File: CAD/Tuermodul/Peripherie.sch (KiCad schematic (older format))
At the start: 43 parts, among them Q201 Q_NPN_CBE, Q202 Q_NPN_CBE, Q203 Q_NPN_CBE, Q204 Q_NPN_CBE, Q205 Q_NPN_CBE, Q206 Q_NPN_CBE, Q207 Q_NPN_CBE, Q208 Q_NPN_CBE, Q209 Q_PMOS_GDS, Q210 Q_PMOS_GDS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

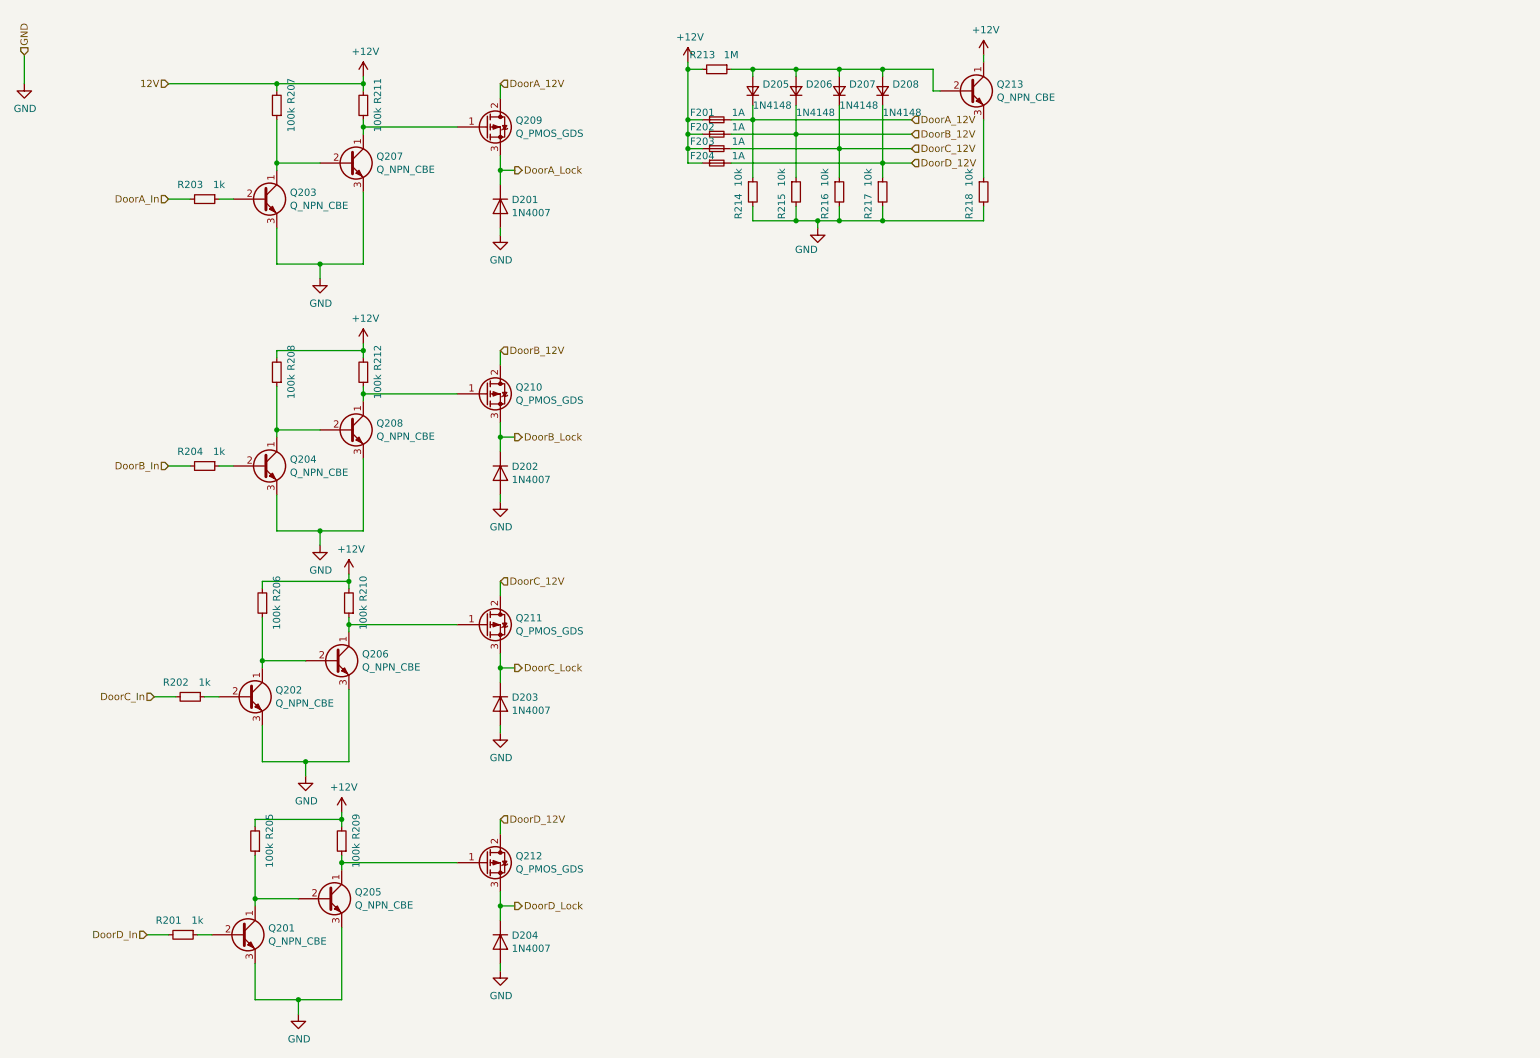
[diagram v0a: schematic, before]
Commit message: -add: Fuse Error, missing LEDs -mod: some Resistor footprints changed -mod: first placement in layout
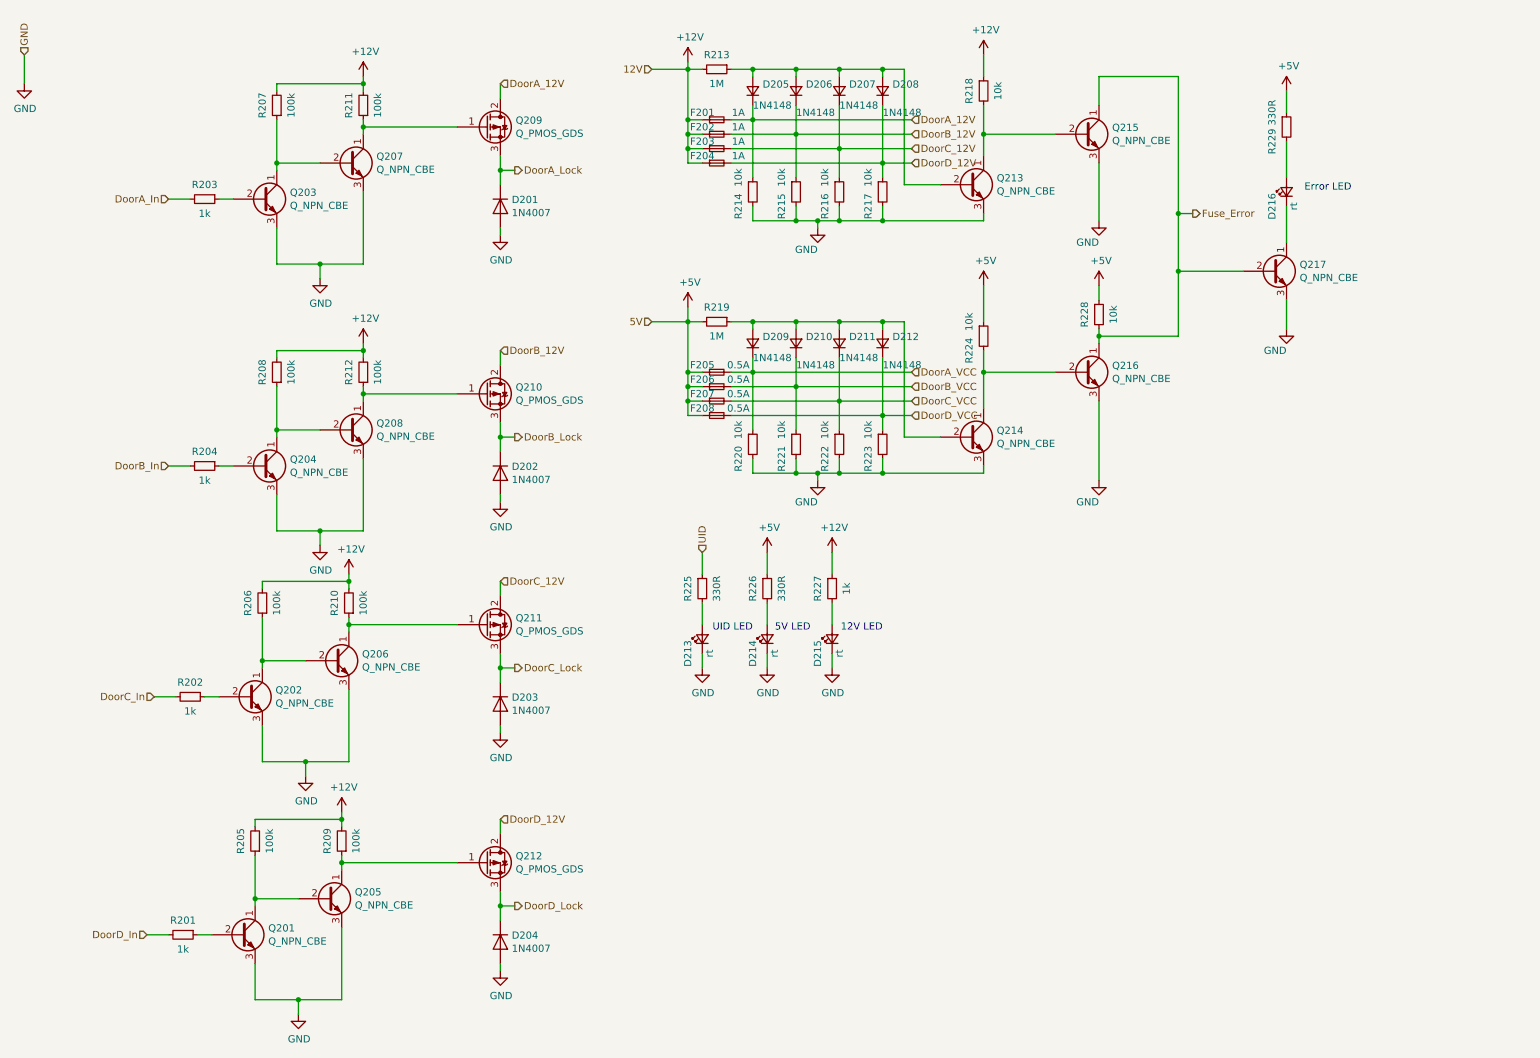
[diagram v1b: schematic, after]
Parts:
- added D209, D210, D211, D212: 1N4148, Diode_THT:D_DO-41_SOD81_P7.62mm_Horizontal, symbol Device:D_Small
- added D213, D214, D215, D216: rt, LED_THT:LED_D3.0mm, symbol Device:LED_Small
- added F205, F206, F207, F208: 0.5A, Fuse:Fuseholder_Cylinder-5x20mm_Schurter_0031_8201_Horizontal_Open, symbol Device:Fuse_Small
- added Q214, Q215, Q216, Q217: Q_NPN_CBE, Package_TO_SOT_THT:TO-92_HandSolder, symbol Device:Q_NPN_CBE
- added R219: 1M, Resistor_THT:R_Axial_DIN0207_L6.3mm_D2.5mm_P7.62mm_Horizontal, symbol Device:R_Small
- added R220, R221, R222, R223, R224, R228: 10k, Resistor_THT:R_Axial_DIN0207_L6.3mm_D2.5mm_P7.62mm_Horizontal, symbol Device:R_Small
- added R225, R226, R229: 330R, Resistor_THT:R_Axial_DIN0207_L6.3mm_D2.5mm_P7.62mm_Horizontal, symbol Device:R_Small
- added R227: 1k, Resistor_THT:R_Axial_DIN0207_L6.3mm_D2.5mm_P7.62mm_Horizontal, symbol Device:R_Small
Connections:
- net +12V: now also R218.1, R227.1; no longer Q213.1 (C)
- net GND: now also Q213.3 (E), D213.1 (K), D214.1 (K), D215.1 (K), Q214.3 (E), Q215.3 (E), Q216.3 (E), Q217.3 (E), R220.2, R221.2, R222.2, R223.2; no longer R218.2
- new net: Q213.1 (C), Q215.2 (B), R218.2
- new net: Q214.1 (C), Q216.2 (B), R224.2
- new net: D209.2 (A), D210.2 (A), D211.2 (A), D212.2 (A), Q214.2 (B), R219.1
- new net: D213.2 (A), R225.2
- new net: D216.1 (K), Q217.1 (C)
- new net: D216.2 (A), R229.2
- new net: D214.2 (A), R226.2
- new net: D215.2 (A), R227.2
- new net +5V: F205.1, F206.1, F207.1, F208.1, R219.2, R224.1, R226.1, R228.1, R229.1
- new net DoorA_VCC: D209.1 (K), F205.2, R220.1
- new net DoorB_VCC: D210.1 (K), F206.2, R221.1
- new net DoorC_VCC: D211.1 (K), F207.2, R222.1
- new net DoorD_VCC: D212.1 (K), F208.2, R223.1
- new net Fuse_Error: Q215.1 (C), Q216.1 (C), Q217.2 (B), R228.2
- new net UID: R225.1
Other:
- note added: "12V LED"
- note added: "5V LED"
- note added: "Error LED"
- note added: "UID LED"
- moved on the sheet: Q213, R218

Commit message: -add: Front.sch for front panel -mod: moved leds and switches to front panel -mod: added MK contacts (not finished jet) -mod: added switches
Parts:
- removed D213, D214, D215, D216: rt, LED_THT:LED_D3.0mm, symbol Device:LED_Small
- removed Q217: Q_NPN_CBE, Package_TO_SOT_THT:TO-92_HandSolder, symbol Device:Q_NPN_CBE
- removed R225, R226, R229: 330R, Resistor_THT:R_Axial_DIN0207_L6.3mm_D2.5mm_P7.62mm_Horizontal, symbol Device:R_Small
- removed R227: 1k, Resistor_THT:R_Axial_DIN0207_L6.3mm_D2.5mm_P7.62mm_Horizontal, symbol Device:R_Small
- added J201: Conn_02x25_Counter_Clockwise, Connector_IDC:IDC-Header_2x25_P2.54mm_Vertical, symbol Connector_Generic:Conn_02x25_Counter_Clockwise
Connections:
- net labels added: 3V3, DA_Rx, DA_Tx, DB_Rx, DB_Tx, DC_Rx, DC_Tx, DD_Rx, DD_Tx, DoorA_Auto, DoorA_MK, DoorB_Auto, DoorB_MK, DoorC_Auto, DoorC_MK, DoorD_Auto, DoorD_MK
- wire segments 221 -> 231
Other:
- note removed: "12V LED"
- note removed: "5V LED"
- note removed: "Error LED"
- note removed: "UID LED"
- moved on the sheet: D201, D202, D203, D204, D205, D206, D207, D208, D209, D210, D211, D212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

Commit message: -add: switch library for spdt switches -mod: improvements in schematic, bugfixes -mod: placement and routing of the ftdi chip + chicken food
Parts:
- removed Q201, Q202, Q203, Q204: Q_NPN_CBE, Package_TO_SOT_THT:TO-92_HandSolder, symbol Device:Q_NPN_CBE
- removed R205, R206, R207, R208: 100k, Resistor_THT:R_Axial_DIN0207_L6.3mm_D2.5mm_P7.62mm_Horizontal, symbol Device:R_Small
- removed R214, R215, R216, R217, R220, R221, R222, R223: 10k, Resistor_THT:R_Axial_DIN0207_L6.3mm_D2.5mm_P7.62mm_Horizontal, symbol Device:R_Small
- added D213, D214: 1N4148, Diode_THT:D_DO-41_SOD81_P7.62mm_Horizontal, symbol Device:D_Small
- added RN201, RN202: 4x10k, Resistor_THT:R_Array_SIP5, symbol Device:R_Network04
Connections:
- net labels removed: 3V3
- wire segments 231 -> 207
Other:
- moved on the sheet: D205, D206, D207, D208, D209, D210, D211, D212, F201, F202, F203, F204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

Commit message: -mod: adapted TechSpec due to power enable discussion -mod: changed pin header for front-to-main panel connection -mod: general layout work
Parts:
- removed J201: Conn_02x25_Counter_Clockwise, Connector_IDC:IDC-Header_2x25_P2.54mm_Vertical, symbol Connector_Generic:Conn_02x25_Counter_Clockwise
- added J201: Conn_02x20_Counter_Clockwise, Connector_PinSocket_2.54mm:PinSocket_2x20_P2.54mm_Vertical_SMD, symbol Connector_Generic:Conn_02x20_Counter_Clockwise
- added R205: 10k, Resistor_SMD:R_0603_1608Metric_Pad1.05x0.95mm_HandSolder, symbol Device:R_Small
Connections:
- net labels added: ~PWR_EN~
- net labels removed: UID
- wire segments 207 -> 212
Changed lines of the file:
@@
 F 3 "~" H 4150 1500 50  0001 C CNN
 	1    4150 1500
-	1    0    0    -1
+	1    0    0    1
 $EndComp
 $Comp
@@
 F 3 "~" H 4150 3350 50  0001 C CNN
 	1    4150 3350
-	1    0    0    -1
+	1    0    0    1
 $EndComp
 Wire Wire Line
@@
 F 3 "~" H 4150 4950 50  0001 C CNN
 	1    4150 4950
-	1    0    0    -1
+	1    0    0    1
 $EndComp
 Wire Wire Line
@@
 F 3 "~" H 4150 6600 50  0001 C CNN
 	1    4150 6600
-	1    0    0    -1
+	1    0    0    1
 $EndComp
 Wire Wire Line
@@
 $EndComp
 $Comp
-L power:GND #PWR?
-U 1 1 5C5F9E5C
-P 3300 4150
-AR Path="/5C5F9E5C" Ref="#PWR?"  Part="1"
-AR Path="/5C5BDAF5/5C5F9E5C" Ref="#PWR0204"  Part="1"
-F 0 "#PWR0204" H 3300 3900 50  0001 C CNN
-F 1 "GND" H 3305 3977 50  0000 C CNN
-F 2 "" H 3300 4150 50  0001 C CNN
-F 3 "" H 3300 4150 50  0001 C CNN
-	1    3300 4150
-	1    0    0    -1
-$EndComp
-$Comp
 L Device:Q_NPN_CBE Q?
 U 1 1 5C5F9E69
@@
 $EndComp
 $Comp
-L power:GND #PWR?
-U 1 1 5C5FAB97
-P 3300 5800
-AR Path="/5C5FAB97" Ref="#PWR?"  Part="1"
-AR Path="/5C5BDAF5/5C5FAB97" Ref="#PWR0202"  Part="1"
-F 0 "#PWR0202" H 3300 5550 50  0001 C CNN
-F 1 "GND" H 3305 5627 50  0000 C CNN
-F 2 "" H 3300 5800 50  0001 C CNN
-F 3 "" H 3300 5800 50  0001 C CNN
-	1    3300 5800
-	1    0    0    -1
-$EndComp
-$Comp
 L Device:R_Small R?
 U 1 1 5C5FABAA
@@
 $EndComp
 $Comp
-L power:GND #PWR?
-U 1 1 5C5FC3EB
-P 3300 7650
-AR Path="/5C5FC3EB" Ref="#PWR?"  Part="1"
-AR Path="/5C5BDAF5/5C5FC3EB" Ref="#PWR0201"  Part="1"
-F 0 "#PWR0201" H 3300 7400 50  0001 C CNN
-F 1 "GND" H 3305 7477 50  0000 C CNN
-F 2 "" H 3300 7650 50  0001 C CNN
-F 3 "" H 3300 7650 50  0001 C CNN
-	1    3300 7650
-	1    0    0    -1
-$EndComp
-$Comp
 L Device:Q_NPN_CBE Q?
 U 1 1 5C5FC3F8
@@
 Wire Wire Line
 	5300 1100 5550 1100
+Text HLabel 10100 4300 0    50   Input ~ 0
+DA_Tx
 Text HLabel 10100 4400 0    50   Input ~ 0
-DA_Tx
-Text HLabel 10100 4500 0    50   Input ~ 0
 DA_Rx
+Text HLabel 10800 4300 2    50   Input ~ 0
+DB_Tx
 Text HLabel 10800 4400 2    50   Input ~ 0
-DB_Tx
-Text HLabel 10800 4500 2    50   Input ~ 0
 DB_Rx
+Text HLabel 10100 5000 0    50   Input ~ 0
+DC_Tx
 Text HLabel 10100 5100 0    50   Input ~ 0
-DC_Tx
-Text HLabel 10100 5200 0    50   Input ~ 0
 DC_Rx
+Text HLabel 10800 5000 2    50   Input ~ 0
+DD_Tx
 Text HLabel 10800 5100 2    50   Input ~ 0
-DD_Tx
-Text HLabel 10800 5200 2    50   Input ~ 0
 DD_Rx
-$Comp
-L Connector_Generic:Conn_02x25_Counter_Clockwise J201
-U 1 1 5C5D89B8
-P 10400 5100
-F 0 "J201" H 10450 6517 50  0000 C CNN
-F 1 "Conn_02x25_Counter_Clockwise" H 10450 6426 50  0000 C CNN
-F 2 "Connector_IDC:IDC-Header_2x25_P2.54mm_Vertical" H 10400 5100 50  0001 C CNN
-F 3 "~" H 10400 5100 50  0001 C CNN
-	1    10400 5100
-	1    0    0    -1
-$EndComp
 $Comp
 L power:+12V #PWR?
@@
 Wire Wire Line
 	10200 4200 10150 4200
-Text HLabel 10150 4300 0    50   Input ~ 0
-UID
-Wire Wire Line
-	10200 4300 10150 4300
-Text HLabel 10100 4600 0    50   Output ~ 0
+Text HLabel 10100 4500 0    50   Output ~ 0
 DoorA_Lock
+Text HLabel 10100 4700 0    50   Input ~ 0
+DoorA_MK
 Text HLabel 10100 4800 0    50   Input ~ 0
-DoorA_MK
+DoorA_12V
 Text HLabel 10100 4900 0    50   Input ~ 0
-DoorA_12V
-Text HLabel 10100 5000 0    50   Input ~ 0
 DoorA_VCC
-Text HLabel 10800 4600 2    50   Output ~ 0
+Text HLabel 10800 4500 2    50   Output ~ 0
 DoorB_Lock
-Text HLabel 10100 5300 0    50   Output ~ 0
+Text HLabel 10100 5200 0    50   Output ~ 0
 DoorC_Lock
-Text HLabel 10800 5300 2    50   Output ~ 0
+Text HLabel 10800 5200 2    50   Output ~ 0
 DoorD_Lock
+Text HLabel 10800 4700 2    50   Input ~ 0
+DoorB_MK
+Text HLabel 10100 5400 0    50   Input ~ 0
+DoorC_MK
+Text HLabel 10800 5400 2    50   Input ~ 0
+DoorD_MK
 Text HLabel 10800 4800 2    50   Input ~ 0
-DoorB_MK
+DoorB_12V
 Text HLabel 10100 5500 0    50   Input ~ 0
-DoorC_MK
+DoorC_12V
 Text HLabel 10800 5500 2    50   Input ~ 0
-DoorD_MK
+DoorD_12V
 Text HLabel 10800 4900 2    50   Input ~ 0
-DoorB_12V
+DoorB_VCC
 Text HLabel 10100 5600 0    50   Input ~ 0
-DoorC_12V
+DoorC_VCC
 Text HLabel 10800 5600 2    50   Input ~ 0
-DoorD_12V
-Text HLabel 10800 5000 2    50   Input ~ 0
-DoorB_VCC
-Text HLabel 10100 5700 0    50   Input ~ 0
-DoorC_VCC
-Text HLabel 10800 5700 2    50   Input ~ 0
 DoorD_VCC
 Text HLabel 4350 1850 2    50   Input ~ 0
@@
 Wire Wire Line
 	4250 2000 4250 2100
-Text HLabel 10100 4700 0    50   Input ~ 0
+Text HLabel 10100 4600 0    50   Input ~ 0
 DoorA_Auto
-Text HLabel 10800 4700 2    50   Input ~ 0
+Text HLabel 10800 4600 2    50   Input ~ 0
 DoorB_Auto
-Text HLabel 10100 5400 0    50   Input ~ 0
+Text HLabel 10100 5300 0    50   Input ~ 0
 DoorC_Auto
-Text HLabel 10800 5400 2    50   Input ~ 0
+Text HLabel 10800 5300 2    50   Input ~ 0
 DoorD_Auto
 Wire Wire Line
@@
 	10100 5600 10200 5600
 Wire Wire Line
-	10100 5700 10200 5700
-Wire Wire Line
-	10800 5700 10700 5700
-Wire Wire Line
 	10700 5600 10800 5600
 Wire Wire Line
@@
 Wire Wire Line
 	9250 2100 9250 2950
-$Comp
-L power:GND #PWR?
-U 1 1 5C5C48A6
-P 3300 2450
-AR Path="/5C5C48A6" Ref="#PWR?"  Part="1"
-AR Path="/5C5BDAF5/5C5C48A6" Ref="#PWR0203"  Part="1"
-F 0 "#PWR0203" H 3300 2200 50  0001 C CNN
-F 1 "GND" H 3305 2277 50  0000 C CNN
-F 2 "" H 3300 2450 50  0001 C CNN
-F 3 "" H 3300 2450 50  0001 C CNN
-	1    3300 2450
-	1    0    0    -1
-$EndComp
 Wire Wire Line
 	3300 7050 3300 7650
@@
 Wire Wire Line
 	6300 3600 6300 3650
+Text HLabel 3200 2450 0    50   Input ~ 0
+~PWR_EN~
+Text HLabel 3200 4150 0    50   Input ~ 0
+~PWR_EN~
+Text HLabel 3200 5800 0    50   Input ~ 0
+~PWR_EN~
+Text HLabel 3200 7650 0    50   Input ~ 0
+~PWR_EN~
+Text HLabel 1400 1300 3    50   Input ~ 0
+~PWR_EN~
+Wire Wire Line
+	3200 2450 3300 2450
+Wire Wire Line
+	3200 4150 3300 4150
+Wire Wire Line
+	3200 5800 3300 5800
+Wire Wire Line
+	3300 7650 3200 7650
+$Comp
+L power:+5V #PWR?
+U 1 1 5C7550B2
+P 1400 900
+AR Path="/5C7550B2" Ref="#PWR?"  Part="1"
+AR Path="/5C5BDAF5/5C7550B2" Ref="#PWR0143"  Part="1"
+F 0 "#PWR0143" H 1400 750 50  0001 C CNN
+F 1 "+5V" H 1400 1050 50  0000 C CNN
+F 2 "" H 1400 900 50  0001 C CNN
+F 3 "" H 1400 900 50  0001 C CNN
+	1    1400 900
+	1    0    0    -1
+$EndComp
+$Comp
+L Device:R_Small R?
+U 1 1 5C7553DD
+P 1400 1100
+AR Path="/5C7553DD" Ref="R?"  Part="1"
+AR Path="/5C5BDAF5/5C7553DD" Ref="R205"  Part="1"
+F 0 "R205" V 1300 1100 50  0000 C CNN
+F 1 "10k" V 1500 1100 50  0000 C CNN
+F 2 "Resistor_SMD:R_0603_1608Metric_Pad1.05x0.95mm_HandSolder" H 1400 1100 50  0001 C CNN
+F 3 "~" H 1400 1100 50  0001 C CNN
+	1    1400 1100
+	1    0    0    -1
+$EndComp
+Wire Wire Line
+	1400 900  1400 1000
+Wire Wire Line
+	1400 1200 1400 1300
+$Comp
+L Connector_Generic:Conn_02x20_Counter_Clockwise J201
+U 1 1 5C76CCF2
+P 10400 4800
+F 0 "J201" H 10450 5917 50  0000 C CNN
+F 1 "Conn_02x20_Counter_Clockwise" H 10450 5826 50  0000 C CNN
+F 2 "Connector_PinSocket_2.54mm:PinSocket_2x20_P2.54mm_Vertical_SMD" H 10400 4800 50  0001 C CNN
+F 3 "~" H 10400 4800 50  0001 C CNN
+	1    10400 4800
+	1    0    0    -1
+$EndComp
+Wire Wire Line
+	10800 4300 10700 4300
+Wire Wire Line
+	10200 4300 10100 4300
 $EndSCHEMATC

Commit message: -mod: Umbelegung Stecker zwischen Haupt und Frontplatine -add: 100n caps für MK Entprellung -mod: Routing Stecker -mod: Platzierung Front nach Vorgabe
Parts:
- added R206, R207, R208, R214, R215, R216, R217, R220, R221, R223, R225, R226: 1k, Resistor_SMD:R_0603_1608Metric_Pad1.05x0.95mm_HandSolder, symbol Device:R_Small
- J201: value Conn_02x20_Counter_Clockwise -> Conn_02x20_Odd_Even; symbol Connector_Generic:Conn_02x20_Counter_Clockwise -> Connector_Generic:Conn_02x20_Odd_Even
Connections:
- net DA_Rx: now also R207.1; no longer J201.6 (Pin_6)
- net DA_Tx: now also R206.1; no longer J201.5 (Pin_5)
- net DB_Rx: now also R221.2; no longer J201.35 (Pin_35)
- net DB_Tx: now also R220.2; no longer J201.36 (Pin_36)
- net DC_Rx: now also R216.1; no longer J201.13 (Pin_13)
- net DC_Tx: now also R215.1; no longer J201.12 (Pin_12)
- net DD_Rx: now also R226.2; no longer J201.28 (Pin_28)
- net DD_Tx: now also R225.2; no longer J201.29 (Pin_29)
- net DoorA_12V: now also J201.13 (Pin_13); no longer J201.10 (Pin_10)
- net DoorA_Auto: now also J201.17 (Pin_17); no longer J201.8 (Pin_8)
- net DoorA_Lock: now also J201.15 (Pin_15); no longer J201.7 (Pin_7)
- net DoorA_MK: now also J201.11 (Pin_11); no longer J201.9 (Pin_9)
- net DoorA_VCC: now also R208.1; no longer J201.11 (Pin_11)
- net DoorB_12V: now also J201.14 (Pin_14); no longer J201.31 (Pin_31)
- net DoorB_Auto: now also J201.18 (Pin_18); no longer J201.33 (Pin_33)
- net DoorB_Lock: now also J201.16 (Pin_16); no longer J201.34 (Pin_34)
- net DoorB_MK: now also J201.12 (Pin_12); no longer J201.32 (Pin_32)
- net DoorB_VCC: now also R217.2; no longer J201.30 (Pin_30)
- net DoorC_12V: now also J201.27 (Pin_27); no longer J201.17 (Pin_17)
- net DoorC_Auto: now also J201.31 (Pin_31); no longer J201.15 (Pin_15)
- net DoorC_Lock: now also J201.29 (Pin_29); no longer J201.14 (Pin_14)
- net DoorC_MK: now also J201.25 (Pin_25); no longer J201.16 (Pin_16)
- net DoorC_VCC: now also R214.1; no longer J201.18 (Pin_18)
- net DoorD_12V: now also J201.28 (Pin_28); no longer J201.24 (Pin_24)
- net DoorD_Auto: now also J201.32 (Pin_32); no longer J201.26 (Pin_26)
- net DoorD_Lock: now also J201.30 (Pin_30); no longer J201.27 (Pin_27)
- net DoorD_MK: now also J201.26 (Pin_26); no longer J201.25 (Pin_25)
- net DoorD_VCC: now also R223.2; no longer J201.23 (Pin_23)
- net Fuse_Error: now also J201.3 (Pin_3); no longer J201.4 (Pin_4)
- net GND: now also J201.33 (Pin_33), J201.34 (Pin_34), J201.35 (Pin_35), J201.36 (Pin_36), J201.37 (Pin_37), J201.38 (Pin_38), J201.39 (Pin_39), J201.4 (Pin_4), J201.40 (Pin_40); no longer J201.3 (Pin_3)
- net at J201.19 (Pin_19): now also R214.2
- net at J201.20 (Pin_20): now also R223.1
- net at J201.21 (Pin_21): now also R215.2
- net at J201.22 (Pin_22): now also R225.1
- new net: J201.10 (Pin_10), R221.1
- new net: J201.23 (Pin_23), R216.2
- new net: J201.24 (Pin_24), R226.1
- new net: J201.5 (Pin_5), R208.2
- new net: J201.6 (Pin_6), R217.1
- new net: J201.7 (Pin_7), R206.2
- new net: J201.8 (Pin_8), R220.1
- new net: J201.9 (Pin_9), R207.2
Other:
- moved on the sheet: J201
